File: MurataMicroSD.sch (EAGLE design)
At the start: 15 parts, among them U1 IC_BLE_LBCA2HNZYZ-711

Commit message: [ uSD ][ SCH ] added RESET node
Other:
- note added: "CC-BY-SA"
- note added: "r03"
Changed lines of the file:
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@@
 <text x="154.94" y="93.98" size="1.778" layer="94">P0_7/MISO</text>
 <text x="71.12" y="114.3" size="1.778" layer="94" rot="MR0" align="center-left">P0_0/!CS!</text>
+<text x="162.56" y="15.24" size="6.4516" layer="94">r03</text>
+<text x="162.56" y="5.08" size="6.4516" layer="94">CC-BY-SA</text>
+<text x="99.06" y="116.84" size="1.778" layer="94" rot="MR0" align="center-left">RESET</text>
 </plain>
 <instances>
@@
 <pinref part="R1" gate="G$1" pin="2"/>
 <wire x1="109.22" y1="114.3" x2="111.76" y2="114.3" width="0.1524" layer="91"/>
+<wire x1="109.22" y1="114.3" x2="109.22" y2="116.84" width="0.1524" layer="91"/>
+<wire x1="109.22" y1="116.84" x2="99.06" y2="116.84" width="0.1524" layer="91"/>
 </segment>
 <segment>

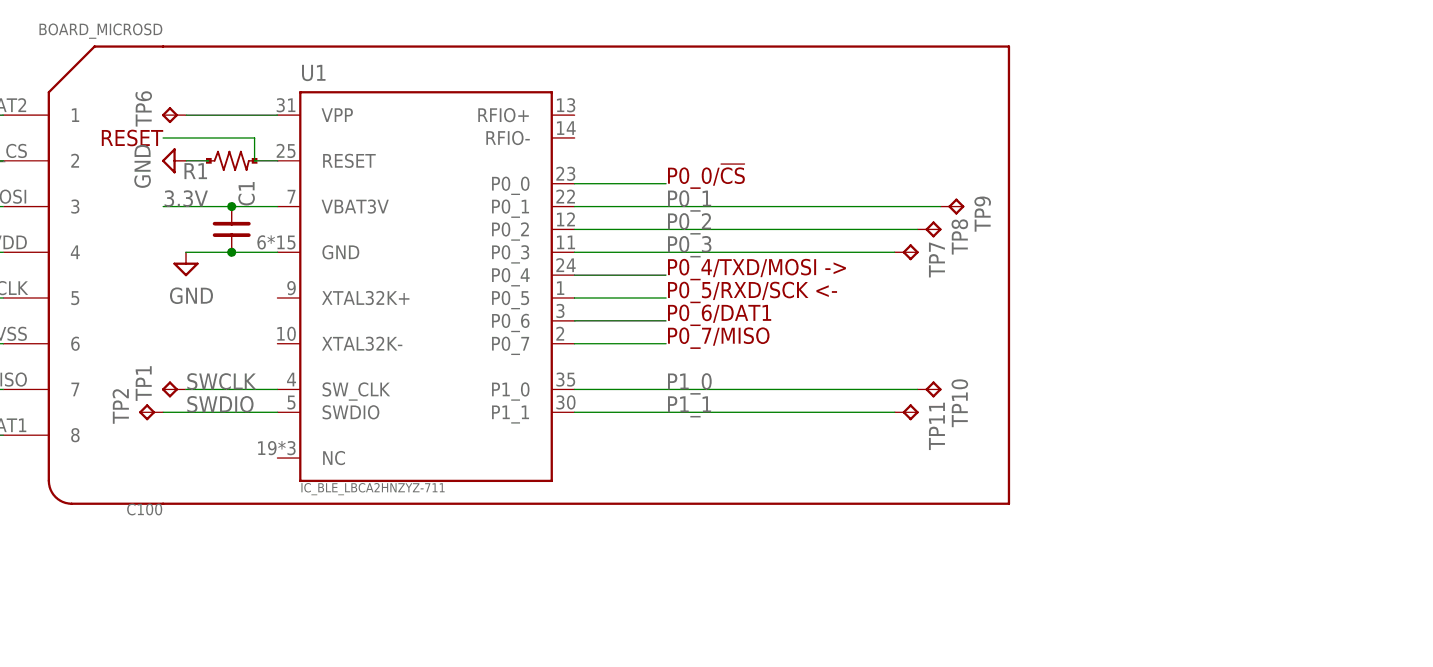
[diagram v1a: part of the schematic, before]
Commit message: [ FIX ] library update; add debug connector
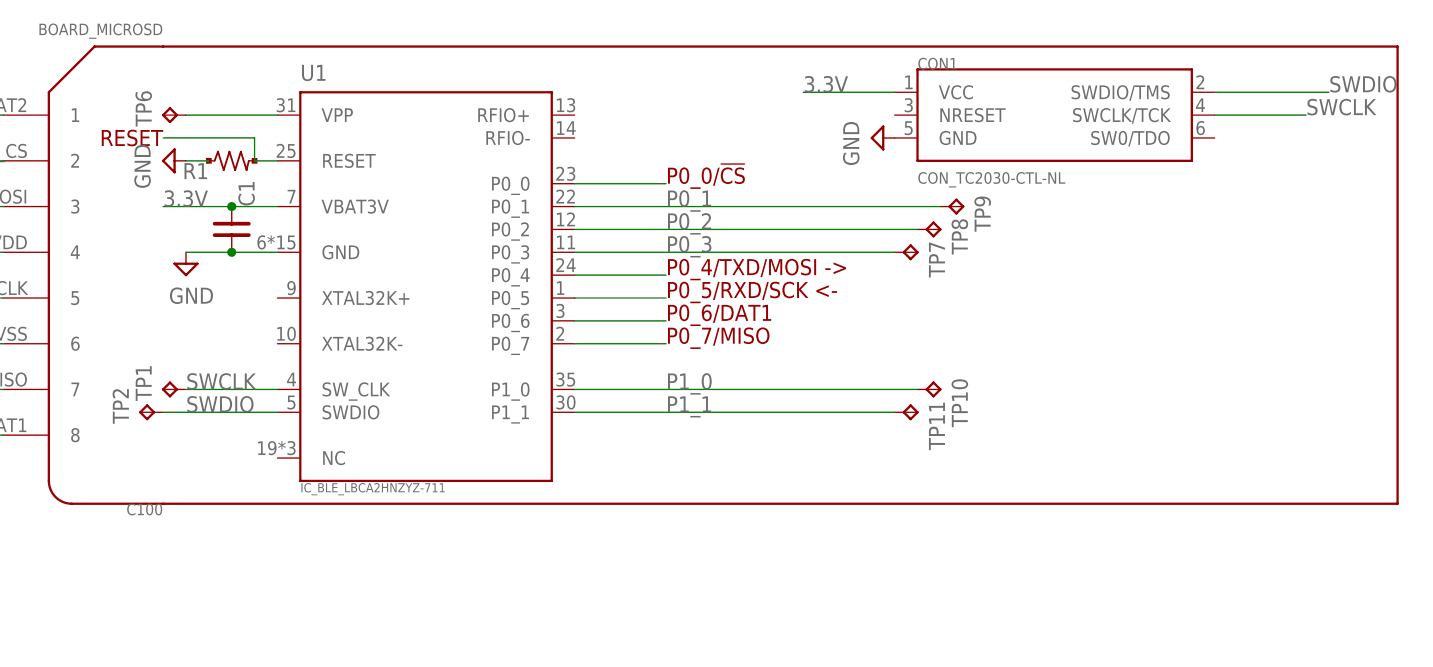
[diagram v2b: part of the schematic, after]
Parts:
- added CON1: CON_TC2030-CTL-NL, mylib:CON_TC2030-CTL-NL
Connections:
- net 3.3V: now also CON1.VCC
- net GND: now also CON1.GND
- net SWCLK: now also CON1.SWCLK/TCK
- net SWDIO: now also CON1.SWDIO/TMS
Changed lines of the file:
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@@
 <layers>
 <layer number="1" name="Top" color="4" fill="1" visible="no" active="no"/>
+<layer number="2" name="Route2" color="1" fill="3" visible="no" active="no"/>
+<layer number="3" name="Route3" color="4" fill="3" visible="no" active="no"/>
+<layer number="14" name="Route14" color="1" fill="6" visible="no" active="no"/>
+<layer number="15" name="Route15" color="4" fill="6" visible="no" active="no"/>
 <layer number="16" name="Bottom" color="1" fill="1" visible="no" active="no"/>
 <layer number="17" name="Pads" color="2" fill="1" visible="no" active="no"/>
@@
 <layer number="132" name="bAdjust" color="7" fill="1" visible="no" active="yes"/>
 <layer number="144" name="Drill_legend" color="7" fill="1" visible="yes" active="yes"/>
+<layer number="145" name="DrillLegend_01-16" color="2" fill="9" visible="no" active="yes"/>
+<layer number="146" name="DrillLegend_01-20" color="3" fill="9" visible="no" active="yes"/>
 <layer number="151" name="HeatSink" color="7" fill="1" visible="yes" active="yes"/>
 <layer number="152" name="_bDocu" color="7" fill="1" visible="yes" active="yes"/>
@@
 <part name="TP10" library="testpad_local" deviceset="TP" device="TP08R"/>
 <part name="TP11" library="testpad_local" deviceset="TP" device="TP08R"/>
+<part name="CON1" library="mylib" deviceset="CON_TC2030" device="-CTL-NL"/>
+<part name="SUPPLY4" library="mylib" deviceset="GND" device=""/>
 </parts>
 <sheets>
@@
 <text x="71.12" y="99.06" size="1.778" layer="94" rot="MR0" align="center-left">-&gt; P0_5/RXD/SCK</text>
 <text x="71.12" y="109.22" size="1.778" layer="94" rot="MR0" align="center-left">&lt;- P0_4/TXD/MOSI</text>
-<wire x1="99.06" y1="76.2" x2="193.04" y2="76.2" width="0.254" layer="94"/>
-<wire x1="193.04" y1="76.2" x2="193.04" y2="127" width="0.254" layer="94"/>
-<wire x1="193.04" y1="127" x2="99.06" y2="127" width="0.254" layer="94"/>
+<wire x1="99.06" y1="76.2" x2="236.22" y2="76.2" width="0.254" layer="94"/>
+<wire x1="236.22" y1="76.2" x2="236.22" y2="127" width="0.254" layer="94"/>
+<wire x1="236.22" y1="127" x2="99.06" y2="127" width="0.254" layer="94"/>
 <text x="71.12" y="88.9" size="1.778" layer="94" rot="MR0" align="center-left">P0_7/MISO</text>
 <text x="71.12" y="83.82" size="1.778" layer="94" rot="MR0" align="center-left">P0_6/DAT1</text>
@@
 <instance part="TP10" gate="G$1" x="185.42" y="88.9" rot="R270"/>
 <instance part="TP11" gate="G$1" x="182.88" y="86.36" rot="R270"/>
+<instance part="CON1" gate="G$1" x="198.12" y="119.38"/>
+<instance part="SUPPLY4" gate="GND" x="177.8" y="116.84" rot="R270"/>
 </instances>
 <busses>
@@
 <junction x="106.68" y="109.22"/>
 </segment>
+<segment>
+<wire x1="180.34" y1="121.92" x2="170.18" y2="121.92" width="0.1524" layer="91"/>
+<pinref part="CON1" gate="G$1" pin="VCC"/>
+<label x="170.18" y="121.92" size="1.778" layer="95"/>
+</segment>
 </net>
 <net name="GND" class="0">
@@
 <wire x1="104.14" y1="114.3" x2="101.6" y2="114.3" width="0.1524" layer="91"/>
 </segment>
+<segment>
+<pinref part="CON1" gate="G$1" pin="GND"/>
+<pinref part="SUPPLY4" gate="GND" pin="GND"/>
+</segment>
 </net>
 <net name="N$1" class="0">
@@
 <pinref part="TP1" gate="G$1" pin="TP"/>
 </segment>
+<segment>
+<wire x1="226.06" y1="119.38" x2="215.9" y2="119.38" width="0.1524" layer="91"/>
+<pinref part="CON1" gate="G$1" pin="SWCLK/TCK"/>
+<label x="226.06" y="119.38" size="1.778" layer="95"/>
+</segment>
 </net>
 <net name="SWDIO" class="0">
@@
 <pinref part="TP2" gate="G$1" pin="TP"/>
 </segment>
-</net>
+<segment>
+<wire x1="228.6" y1="121.92" x2="215.9" y2="121.92" width="0.1524" layer="91"/>
+<pinref part="CON1" gate="G$1" pin="SWDIO/TMS"/>
+<label x="228.6" y="121.92" size="1.778" layer="95"/>
+</segment>
+</net>

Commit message: [ uSD ] add 'Open Source Hardware' silk
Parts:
- removed TP1, TP2: TPTP08R, testpad_local:TPTP08R
- TP3, TP4, TP5: value TPTP08R -> TPTP20R; device testpad_local:TPTP08R -> testpad_local:TPTP20R
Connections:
- net SWCLK: no longer TP1.TP
- net SWDIO: no longer TP2.TP
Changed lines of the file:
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@@
 <part name="R1" library="mylib" deviceset="R_US_PAD_PAD" device="_1005"/>
 <part name="SUPPLY3" library="mylib" deviceset="GND" device=""/>
-<part name="TP1" library="testpad_local" deviceset="TP" device="TP08R"/>
-<part name="TP2" library="testpad_local" deviceset="TP" device="TP08R"/>
-<part name="TP3" library="testpad_local" deviceset="TP" device="TP08R"/>
-<part name="TP4" library="testpad_local" deviceset="TP" device="TP08R"/>
-<part name="TP5" library="testpad_local" deviceset="TP" device="TP08R"/>
+<part name="TP3" library="testpad_local" deviceset="TP" device="TP20R" value="TPTP20R"/>
+<part name="TP4" library="testpad_local" deviceset="TP" device="TP20R" value="TPTP20R"/>
+<part name="TP5" library="testpad_local" deviceset="TP" device="TP20R" value="TPTP20R"/>
 <part name="TP6" library="testpad_local" deviceset="TP" device="TP08R"/>
 <part name="TP7" library="testpad_local" deviceset="TP" device="TP08R"/>
@@
 <instance part="R1" gate="G$1" x="106.68" y="114.3"/>
 <instance part="SUPPLY3" gate="GND" x="99.06" y="114.3" rot="R270"/>
-<instance part="TP1" gate="G$1" x="99.06" y="88.9" rot="R90"/>
-<instance part="TP2" gate="G$1" x="96.52" y="86.36" rot="R90"/>
 <instance part="TP3" gate="G$1" x="223.52" y="43.18" rot="R90"/>
 <instance part="TP4" gate="G$1" x="223.52" y="38.1" rot="R90"/>
@@
 <wire x1="111.76" y1="88.9" x2="101.6" y2="88.9" width="0.1524" layer="91"/>
 <label x="101.6" y="88.9" size="1.778" layer="95"/>
-<pinref part="TP1" gate="G$1" pin="TP"/>
-</segment>
-<segment>
-<wire x1="226.06" y1="119.38" x2="215.9" y2="119.38" width="0.1524" layer="91"/>
+</segment>
+<segment>
+<wire x1="223.52" y1="119.38" x2="215.9" y2="119.38" width="0.1524" layer="91"/>
 <pinref part="CON1" gate="G$1" pin="SWCLK/TCK"/>
-<label x="226.06" y="119.38" size="1.778" layer="95"/>
+<label x="223.52" y="119.38" size="1.778" layer="95"/>
 </segment>
 </net>
@@
 <segment>
 <pinref part="U1" gate="G$1" pin="SWDIO"/>
-<wire x1="111.76" y1="86.36" x2="99.06" y2="86.36" width="0.1524" layer="91"/>
+<wire x1="111.76" y1="86.36" x2="101.6" y2="86.36" width="0.1524" layer="91"/>
 <label x="101.6" y="86.36" size="1.778" layer="95"/>
-<pinref part="TP2" gate="G$1" pin="TP"/>
-</segment>
-<segment>
-<wire x1="228.6" y1="121.92" x2="215.9" y2="121.92" width="0.1524" layer="91"/>
+</segment>
+<segment>
+<wire x1="223.52" y1="121.92" x2="215.9" y2="121.92" width="0.1524" layer="91"/>
 <pinref part="CON1" gate="G$1" pin="SWDIO/TMS"/>
-<label x="228.6" y="121.92" size="1.778" layer="95"/>
-</segment>
-</net>
+<label x="223.52" y="121.92" size="1.778" layer="95"/>
+</segment>
+</net>

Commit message: [ uSD ] uSD pin 8 is replaced to Vpp
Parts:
- removed TP6: TPTP08R, testpad_local:TPTP08R
- added TP1: TPTP08R, testpad_local:TPTP08R
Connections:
- net DAT1: now also TP1.TP; no longer C100.8
- net N$2: now also C100.8; no longer TP6.TP
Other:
- note added: "VPP"
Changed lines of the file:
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@@
 <part name="TP4" library="testpad_local" deviceset="TP" device="TP20R" value="TPTP20R"/>
 <part name="TP5" library="testpad_local" deviceset="TP" device="TP20R" value="TPTP20R"/>
-<part name="TP6" library="testpad_local" deviceset="TP" device="TP08R"/>
 <part name="TP7" library="testpad_local" deviceset="TP" device="TP08R"/>
 <part name="TP8" library="testpad_local" deviceset="TP" device="TP08R"/>
@@
 <part name="CON1" library="mylib" deviceset="CON_TC2030" device="-CTL-NL"/>
 <part name="SUPPLY4" library="mylib" deviceset="GND" device=""/>
+<part name="TP1" library="testpad_local" deviceset="TP" device="TP08R"/>
 </parts>
 <sheets>
@@
 <wire x1="236.22" y1="127" x2="99.06" y2="127" width="0.254" layer="94"/>
 <text x="71.12" y="88.9" size="1.778" layer="94" rot="MR0" align="center-left">P0_7/MISO</text>
-<text x="71.12" y="83.82" size="1.778" layer="94" rot="MR0" align="center-left">P0_6/DAT1</text>
 <text x="154.94" y="93.98" size="1.778" layer="94">P0_7/MISO</text>
 <text x="71.12" y="114.3" size="1.778" layer="94" rot="MR0" align="center-left">P0_0/!CS!</text>
@@
 <text x="162.56" y="5.08" size="6.4516" layer="94">CC-BY-SA</text>
 <text x="99.06" y="116.84" size="1.778" layer="94" rot="MR0" align="center-left">RESET</text>
+<text x="101.6" y="119.38" size="1.778" layer="94" rot="MR0" align="center-left">VPP</text>
+<text x="71.12" y="83.82" size="1.778" layer="94" rot="MR0" align="center-left">VPP</text>
 </plain>
 <instances>
@@
 <instance part="TP4" gate="G$1" x="223.52" y="38.1" rot="R90"/>
 <instance part="TP5" gate="G$1" x="223.52" y="33.02" rot="R90"/>
-<instance part="TP6" gate="G$1" x="99.06" y="119.38" rot="R90"/>
 <instance part="TP7" gate="G$1" x="182.88" y="104.14" rot="R270"/>
 <instance part="TP8" gate="G$1" x="185.42" y="106.68" rot="R270"/>
@@
 <instance part="CON1" gate="G$1" x="198.12" y="119.38"/>
 <instance part="SUPPLY4" gate="GND" x="177.8" y="116.84" rot="R270"/>
+<instance part="TP1" gate="G$1" x="172.72" y="96.52" rot="R270"/>
 </instances>
 <busses>
@@
 <net name="DAT1" class="0">
 <segment>
-<wire x1="81.28" y1="83.82" x2="71.12" y2="83.82" width="0.1524" layer="91"/>
-<pinref part="C100" gate="G$1" pin="8"/>
-</segment>
-<segment>
-<wire x1="154.94" y1="96.52" x2="144.78" y2="96.52" width="0.1524" layer="91"/>
+<wire x1="170.18" y1="96.52" x2="144.78" y2="96.52" width="0.1524" layer="91"/>
 <pinref part="U1" gate="G$1" pin="P0_6"/>
+<pinref part="TP1" gate="G$1" pin="TP"/>
 </segment>
 </net>
@@
 <net name="N$2" class="0">
 <segment>
-<pinref part="TP6" gate="G$1" pin="TP"/>
 <pinref part="U1" gate="G$1" pin="VPP"/>
 <wire x1="101.6" y1="119.38" x2="111.76" y2="119.38" width="0.1524" layer="91"/>
 </segment>
-</net>
+<segment>
+<wire x1="71.12" y1="83.82" x2="81.28" y2="83.82" width="0.1524" layer="91"/>
+<pinref part="C100" gate="G$1" pin="8"/>
+</segment>
+</net>

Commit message: [ uSD ][ USB ] library update
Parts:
- removed TP3, TP4, TP5: TPTP20R, testpad_local:TPTP20R
- added TP100, TP101, TP102: TPTP20R, testpad_local:TPTP20R
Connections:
- net DAT1 renamed P0_6
- net N$2 renamed VPP
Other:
- note removed: "P0_6/DAT1"
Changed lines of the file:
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@@
 <part name="R1" library="mylib" deviceset="R_US_PAD_PAD" device="_1005"/>
 <part name="SUPPLY3" library="mylib" deviceset="GND" device=""/>
-<part name="TP3" library="testpad_local" deviceset="TP" device="TP20R" value="TPTP20R"/>
-<part name="TP4" library="testpad_local" deviceset="TP" device="TP20R" value="TPTP20R"/>
-<part name="TP5" library="testpad_local" deviceset="TP" device="TP20R" value="TPTP20R"/>
+<part name="TP100" library="testpad_local" deviceset="TP" device="TP20R" value="TPTP20R"/>
+<part name="TP101" library="testpad_local" deviceset="TP" device="TP20R" value="TPTP20R"/>
+<part name="TP102" library="testpad_local" deviceset="TP" device="TP20R" value="TPTP20R"/>
 <part name="TP7" library="testpad_local" deviceset="TP" device="TP08R"/>
 <part name="TP8" library="testpad_local" deviceset="TP" device="TP08R"/>
@@
 <sheet>
 <plain>
-<circle x="223.52" y="38.1" radius="12.7" width="0.1524" layer="91"/>
-<text x="218.44" y="27.94" size="1.778" layer="91">FIDUCIAL</text>
+<text x="236.22" y="30.48" size="1.778" layer="91">FIDUCIAL</text>
 <text x="154.94" y="111.76" size="1.778" layer="94">P0_0/!CS!</text>
 <text x="154.94" y="101.6" size="1.778" layer="94">P0_4/TXD/MOSI -&gt;</text>
 <text x="154.94" y="99.06" size="1.778" layer="94">P0_5/RXD/SCK &lt;-</text>
-<text x="154.94" y="96.52" size="1.778" layer="94">P0_6/DAT1</text>
 <text x="71.12" y="119.38" size="1.778" layer="94" rot="MR0" align="center-left">RESET</text>
 <text x="71.12" y="99.06" size="1.778" layer="94" rot="MR0" align="center-left">-&gt; P0_5/RXD/SCK</text>
@@
 <text x="101.6" y="119.38" size="1.778" layer="94" rot="MR0" align="center-left">VPP</text>
 <text x="71.12" y="83.82" size="1.778" layer="94" rot="MR0" align="center-left">VPP</text>
+<circle x="241.3" y="40.64" radius="15.24" width="0.1524" layer="91"/>
 </plain>
 <instances>
@@
 <instance part="R1" gate="G$1" x="106.68" y="114.3"/>
 <instance part="SUPPLY3" gate="GND" x="99.06" y="114.3" rot="R270"/>
-<instance part="TP3" gate="G$1" x="223.52" y="43.18" rot="R90"/>
-<instance part="TP4" gate="G$1" x="223.52" y="38.1" rot="R90"/>
-<instance part="TP5" gate="G$1" x="223.52" y="33.02" rot="R90"/>
+<instance part="TP100" gate="G$1" x="231.14" y="43.18"/>
+<instance part="TP101" gate="G$1" x="238.76" y="43.18"/>
+<instance part="TP102" gate="G$1" x="246.38" y="43.18"/>
 <instance part="TP7" gate="G$1" x="182.88" y="104.14" rot="R270"/>
 <instance part="TP8" gate="G$1" x="185.42" y="106.68" rot="R270"/>
@@
 </segment>
 </net>
-<net name="DAT1" class="0">
+<net name="P0_6" class="0">
 <segment>
 <wire x1="170.18" y1="96.52" x2="144.78" y2="96.52" width="0.1524" layer="91"/>
 <pinref part="U1" gate="G$1" pin="P0_6"/>
 <pinref part="TP1" gate="G$1" pin="TP"/>
+<label x="154.94" y="96.52" size="1.778" layer="95"/>
 </segment>
 </net>
@@
 </segment>
 </net>
-<net name="N$2" class="0">
+<net name="VPP" class="0">
 <segment>
 <pinref part="U1" gate="G$1" pin="VPP"/>
